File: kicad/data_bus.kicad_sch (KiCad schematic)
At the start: 15 parts, among them U18 SN74F377AN, U26 SN74F541N, U27 SN74F541N

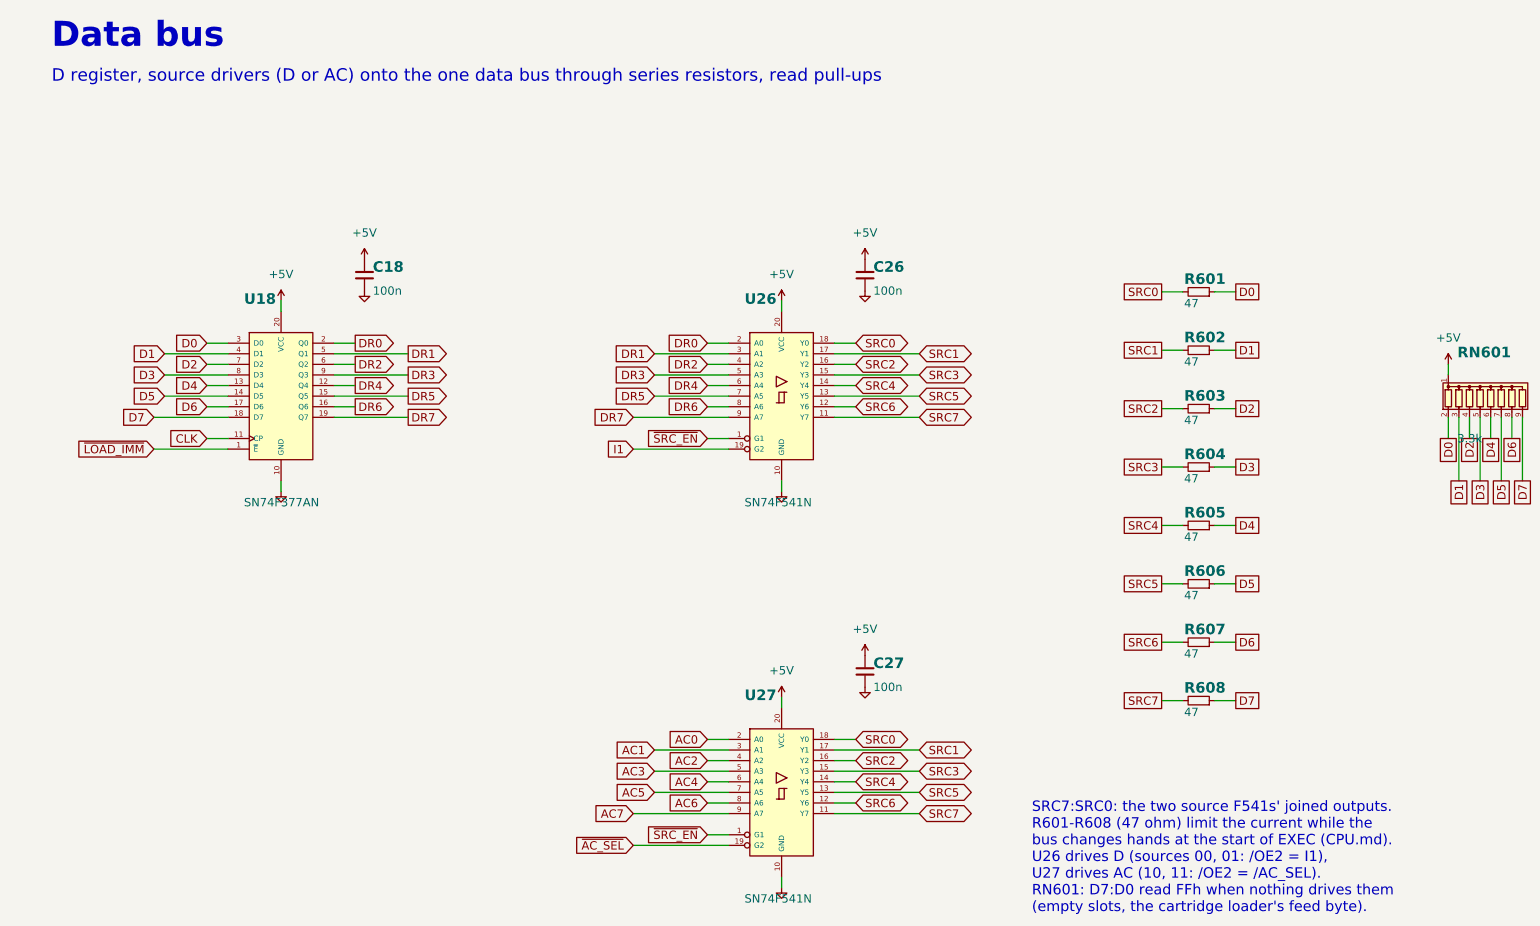
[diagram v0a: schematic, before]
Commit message: KiCad schematic: wire each sheet's nets, one routed bus per bus, PLD names
A net with two or more pins on a sheet is now wired pin to pin by a small
grid router (src/scripts/kicad_route.py) instead of a label per pin.
Numbered groups (D, A, SRC, PC, ...) are drawn as one bus per sheet with
bus entries, routed between the chips and named by one bus label.  Each
PLD shows its job under its part number.  Netlist check: 0 problems.

Co-Authored-By: Claude Opus 5.5 (1M context) <noreply@anthropic.com>
Claude-Session: https://claude.ai/code/session_01L9AkLuEg13EebxDmgXsaEp
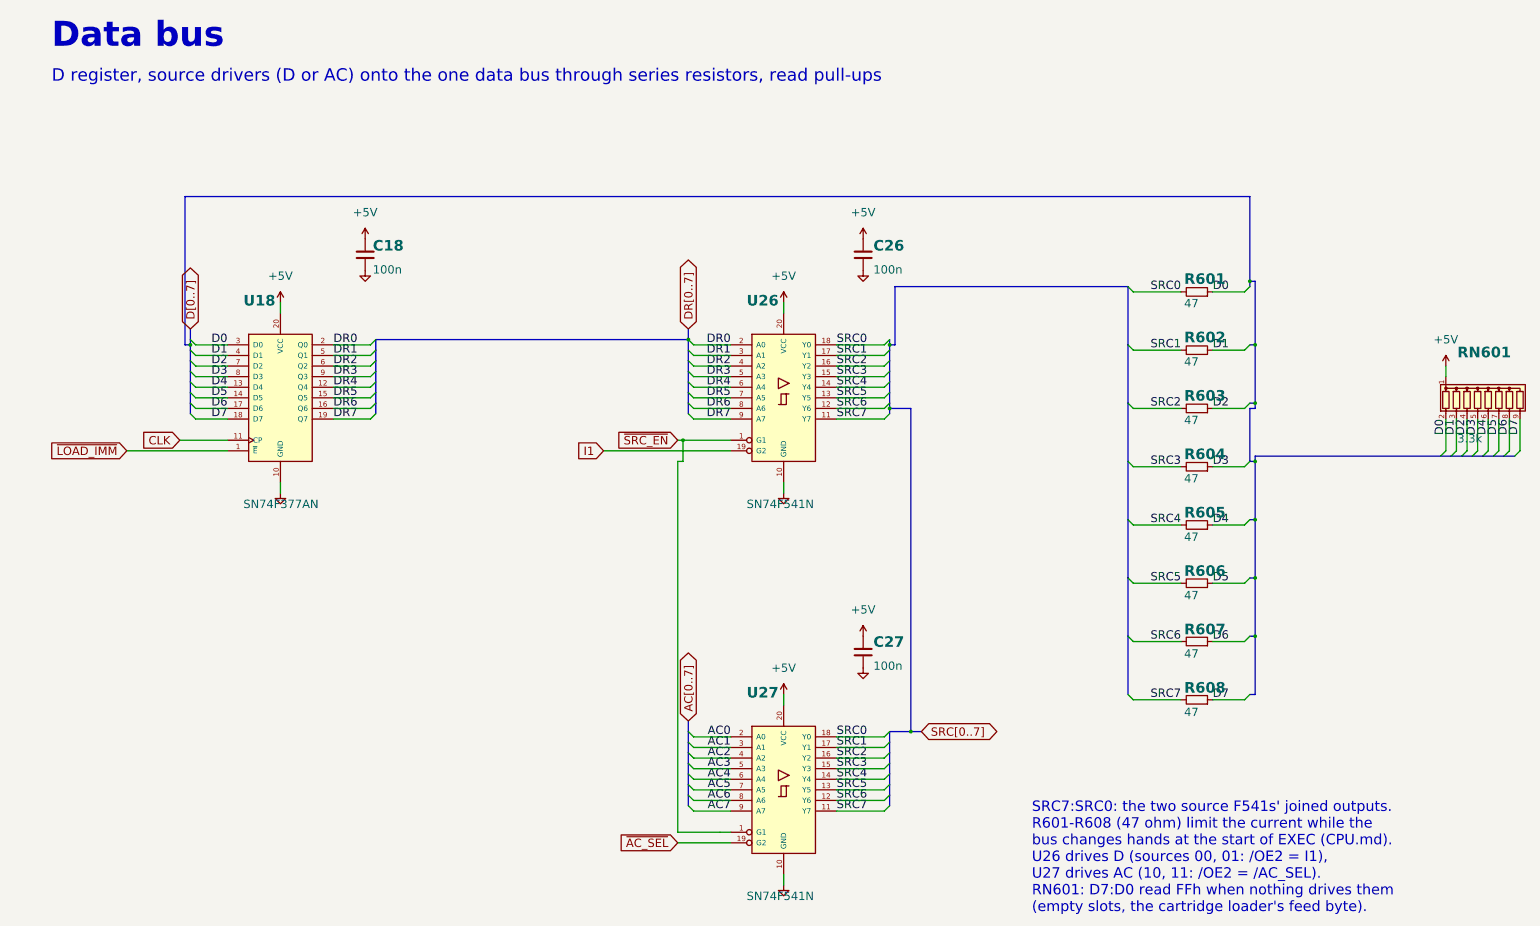
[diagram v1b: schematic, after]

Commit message: Revert the opcode XOR: plain encoding, the cartridge 74AC541 is back
Justin found the inverted opcode bytes too confusing, and a pulled-low
bus is not practical, so this undoes 63a428c:
- opcode bytes are the plain fields again (nop = 02h); the cartridge's
  74AC541 drives 02h while it loads (6 chips, about 33 ms)
- State and Branch PLD revision 15, ALU revision 07 and cartridge PLD
  revision 03 have the same logic as 13, 13, 05 and 01
- read bus pull-ups 10k again; bring-up colour pull-downs 1k
- cartridge schematic gets U6 (74AC541), data bus SIP 10k
- program hex, menu ROM and bring-up ROM reassembled

Kept from 63a428c: RUN starts high in basys_top, the bring-up ROM's
explicit jump to frame_loop, and test_io's con_gets ROM map.

Co-Authored-By: Claude Opus 5.5 (1M context) <noreply@anthropic.com>
Claude-Session: https://claude.ai/code/session_01PNJoPfzmo1tu8EorCrua96
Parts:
- RN601: value 3.3k -> 10k
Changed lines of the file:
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@@
 (kicad_sch (version 20230121) (generator eeschema)
   (paper "A3")
-  (title_block (title "Placard: Data bus") (date "2026-10-20") (rev "1") (company "Placard computer") (comment 1 "Generated by src/scripts/gen_kicad_schematic.py; plan in docs/SCHEMATIC_PLAN.md") (comment 2 "Chip numbers U1-U41 = docs/CHIPS.md; decoupling Cn goes with Un"))
+  (title_block (title "Placard: Data bus") (date "2026-10-21") (rev "1") (company "Placard computer") (comment 1 "Generated by src/scripts/gen_kicad_schematic.py; plan in docs/SCHEMATIC_PLAN.md") (comment 2 "Chip numbers U1-U41 = docs/CHIPS.md; decoupling Cn goes with Un"))
   (text "Data bus" (at 15 22 0) (effects (font (size 6 6) bold) (justify left bottom)))
   (text "D register, source drivers (D or AC) onto the one data bus through series resistors, read pull-ups" (at 15 30 0) (effects (font (size 3 3)) (justify left bottom)))
@@
   (wire (pts (xy 349.25 100.33) (xy 349.25 97.79)) (stroke (width 0) (type default)))
   (symbol (lib_id "power:+5V") (at 349.25 97.79 0) (unit 1) (in_bom yes) (on_board yes) (dnp no) (property "Reference" "#PWR0613" (at 349.25 97.79 0) (effects (font (size 1.27 1.27)) hide)) (property "Value" "+5V" (at 349.25 91.44 0) (effects (font (size 2 2)))) (property "Footprint" "" (at 349.25 97.79 0) (effects (font (size 1.27 1.27)) hide)) (property "Datasheet" "" (at 349.25 97.79 0) (effects (font (size 1.27 1.27)) hide)) (pin "1") (instances (project "placard" (path "/e3450542-4ffc-59d4-a4a7-45636233928a/4ad271a0-c6b7-5e11-9210-343daaa95f9a" (reference "#PWR0613") (unit 1)))))
-  (symbol (lib_id "Device:R_Network08") (at 359.41 105.41 0) (unit 1) (in_bom yes) (on_board yes) (dnp no) (property "Reference" "RN601" (at 352 96 0) (effects (font (size 2.54 2.54) bold) (justify left bottom))) (property "Value" "3.3k" (at 352 114 0) (effects (font (size 2 2)) (justify left top))) (property "Footprint" "Resistor_THT:R_Array_SIP9" (at 359.41 105.41 0) (effects (font (size 1.27 1.27)) hide)) (property "Datasheet" "http://www.vishay.com/docs/31509/csc.pdf" (at 359.41 105.41 0) (effects (font (size 1.27 1.27)) hide)) (pin "1") (pin "2") (pin "3") (pin "4") (pin "5") (pin "6") (pin "7") (pin "8") (pin "9") (instances (project "placard" (path "/e3450542-4ffc-59d4-a4a7-45636233928a/4ad271a0-c6b7-5e11-9210-343daaa95f9a" (reference "RN601") (unit 1)))))
+  (symbol (lib_id "Device:R_Network08") (at 359.41 105.41 0) (unit 1) (in_bom yes) (on_board yes) (dnp no) (property "Reference" "RN601" (at 352 96 0) (effects (font (size 2.54 2.54) bold) (justify left bottom))) (property "Value" "10k" (at 352 114 0) (effects (font (size 2 2)) (justify left top))) (property "Footprint" "Resistor_THT:R_Array_SIP9" (at 359.41 105.41 0) (effects (font (size 1.27 1.27)) hide)) (property "Datasheet" "http://www.vishay.com/docs/31509/csc.pdf" (at 359.41 105.41 0) (effects (font (size 1.27 1.27)) hide)) (pin "1") (pin "2") (pin "3") (pin "4") (pin "5") (pin "6") (pin "7") (pin "8") (pin "9") (instances (project "placard" (path "/e3450542-4ffc-59d4-a4a7-45636233928a/4ad271a0-c6b7-5e11-9210-343daaa95f9a" (reference "RN601") (unit 1)))))
   (text "SRC7:SRC0: the two source F541s' joined outputs." (at 250 205 0) (effects (font (size 2.5 2.5)) (justify left bottom)))
   (text "R601-R608 (47 ohm) limit the current while the" (at 250 209 0) (effects (font (size 2.5 2.5)) (justify left bottom)))
